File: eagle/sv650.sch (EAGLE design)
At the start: 31 parts, among them Q1 IRLML6344

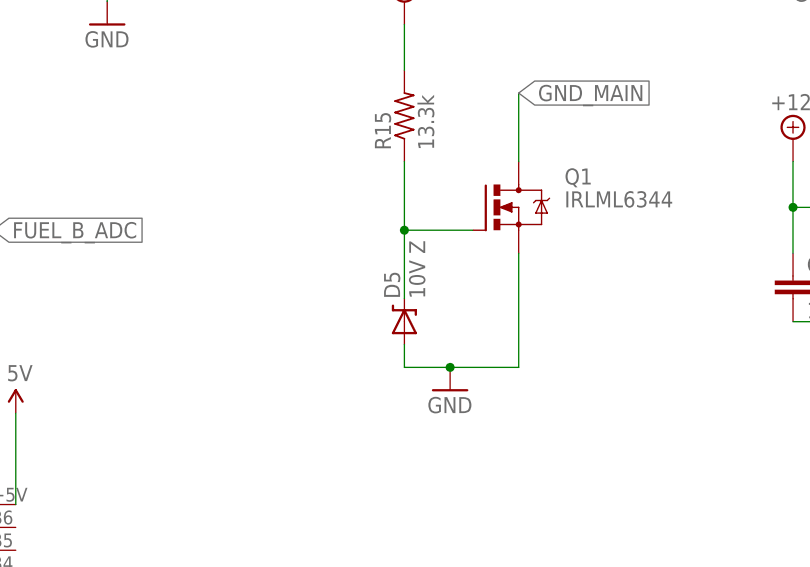
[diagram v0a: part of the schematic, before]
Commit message: switch D5 to a SOD-123 package
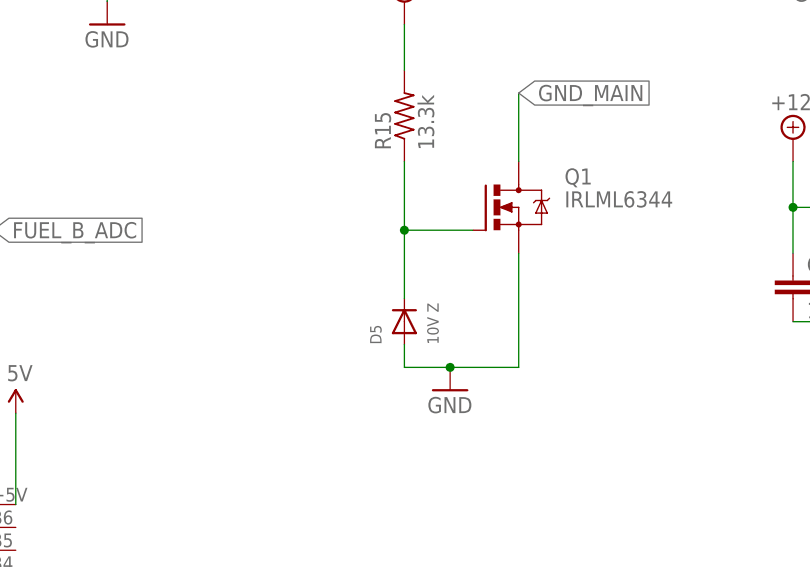
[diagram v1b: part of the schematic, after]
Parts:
- D5: device SparkFun-DiscreteSemi:DIODE-ZENER-BZT52 -> adafruit:DIODESOD-123
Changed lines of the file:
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@@
 <?xml version="1.0" encoding="utf-8"?>
 <!DOCTYPE eagle SYSTEM "eagle.dtd">
-<eagle version="6.5.0">
+<eagle version="7.1.0">
 <drawing>
 <settings>
@@
 <part name="R15" library="resistor" deviceset="R-US_" device="M0805" value="13.3k"/>
 <part name="SUPPLY5" library="supply2" deviceset="+12V" device=""/>
-<part name="D5" library="SparkFun-DiscreteSemi" deviceset="DIODE-ZENER" device="-BZT52" value="10V Z"/>
+<part name="D5" library="adafruit" deviceset="DIODE" device="SOD-123" value="10V Z"/>
 <part name="GND13" library="SparkFun" deviceset="GND" device=""/>
 </parts>

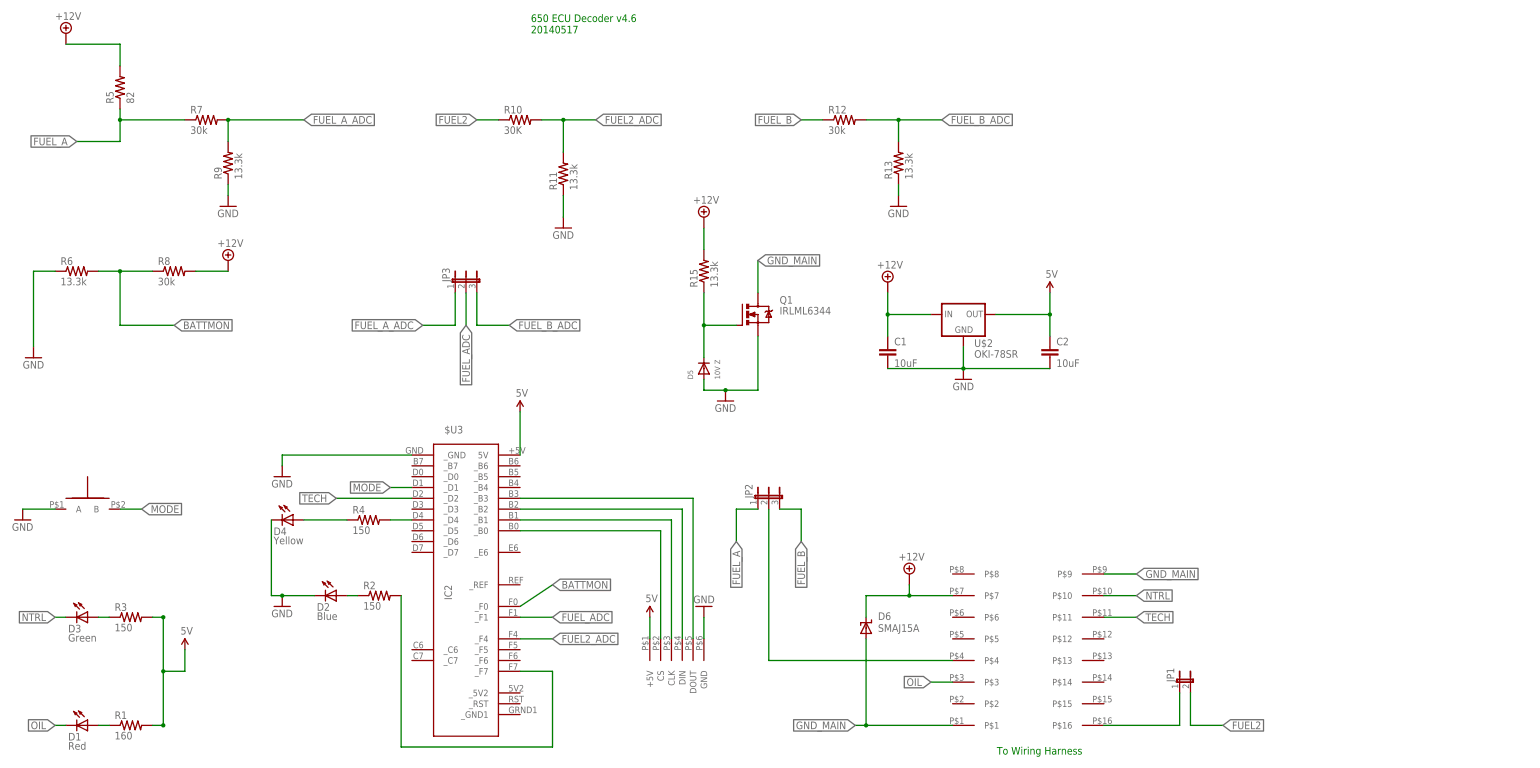
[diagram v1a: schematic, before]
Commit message: First pass at using Nokia LCD display
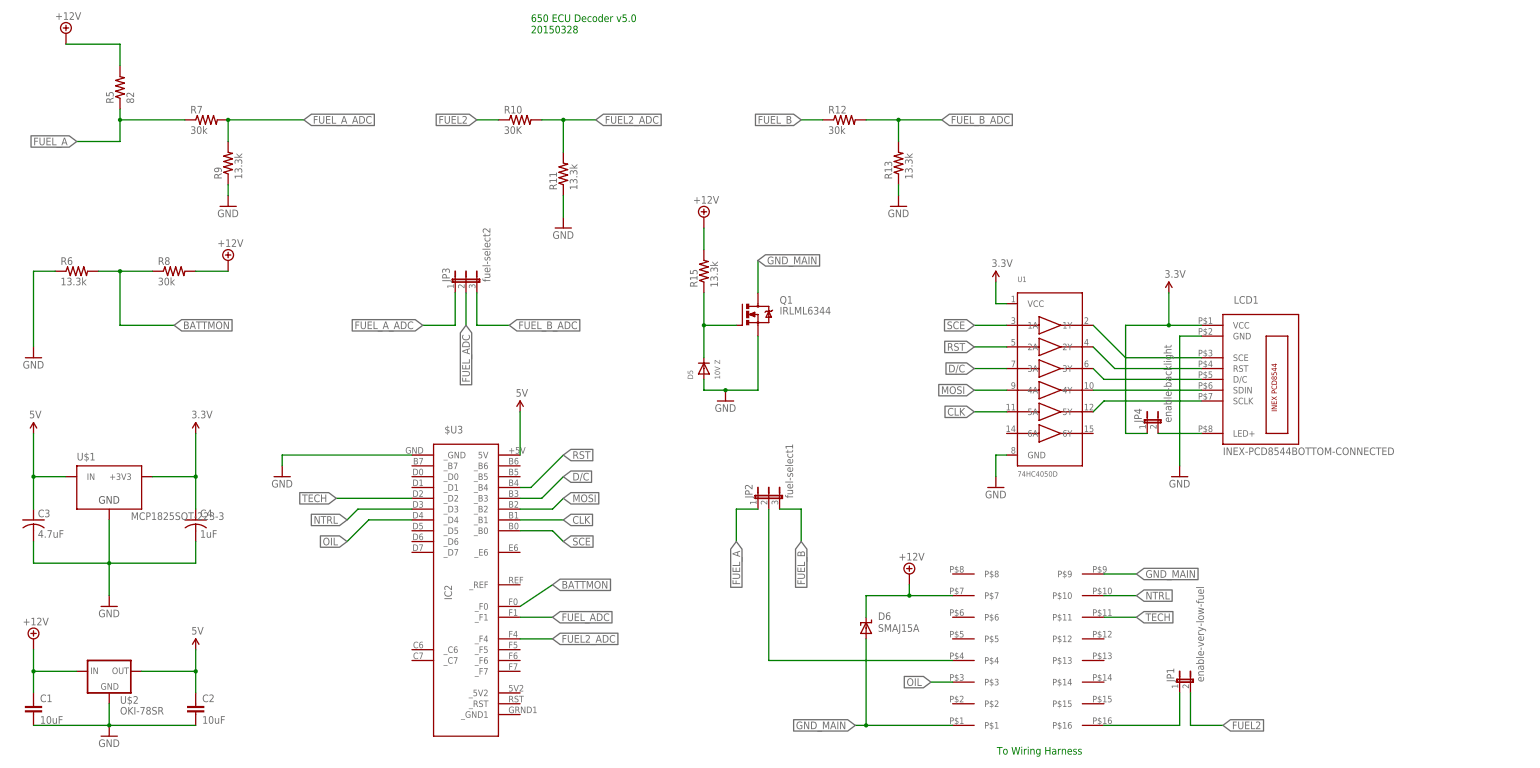
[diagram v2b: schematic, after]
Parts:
- removed D1: Red, led:LED10MM
- removed D2: Blue, led:LED5MM
- removed D3: Green, led:LED10MM
- removed D4: Yellow, led:LED10MM
- removed R1: 160, resistor:R-US_M0805
- removed R2, R3, R4: 150, resistor:R-US_M0805
- removed U$10: R13-509A-05-BB/R13-509A-05-BR, synfinatic:R13-509A-05-BB/R13-509A-05-BR
- added C3: 4.7uF, resistor:C-USC0805
- added C4: 1uF, resistor:C-USC0805
- added JP4: enable-backlight, jumper:JP1E
- added LCD1: INEX-PCD8544BOTTOM-CONNECTED, synfinatic:INEX-PCD8544BOTTOM-CONNECTED
- added U1: 74HC4050D, microbuilder:74HC4050D
- JP1: value (none) -> enable-very-low-fuel
- JP2: value (none) -> fuel-select1
- JP3: value (none) -> fuel-select2
- U$1: value OASIS-7-SEG-DISPLAY -> MCP1825SOT-223-3; device synfinatic:OASIS-7-SEG-DISPLAY -> synfinatic:MCP1825SOT-223-3; OC_NEWARK unknown -> (none)
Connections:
- removed net MODE: $U3._D1, U$10.B
- removed net N$3: $U3._B1, U$1.CLK
- removed net N$4: $U3._B2, U$1.DIN
- removed net N$5: $U3._B3, U$1.DOUT
- removed net N$6: D3.A, R3.1
- removed net N$7: D2.A, R2.1
- removed net R2: D4.A, R4.1
- new net 3.3V: C4.1, JP4.1, LCD1.VCC, U$1.+3V3, U1.VCC
- new net CLK: $U3._B1, U1.5A
- new net D/C: $U3._B3, U1.3A
- new net MOSI: $U3._B2, U1.4A
- new net N$13: LCD1.D/C, U1.3Y
- new net N$15: LCD1.SDIN, U1.4Y
- new net RST: $U3._B4, U1.2A
- new net SCE: $U3._B0, U1.1A
- net 5V: now also C3.1, U$1.IN; no longer R1.2, R3.2, U$1.+5V
- net GND: now also C3.2, C4.2, LCD1.GND, U1.GND; no longer D2.C, D4.C, U$10.A
- net N$16: now also LCD1.SCLK, U1.5Y; no longer $U3._F7, R2.2
- net N$2: now also JP4.2, LCD1.LED+; no longer $U3._B0, U$1.CS
- net N$8: now also LCD1.SCE, U1.1Y; no longer D1.A, R1.1
- net N$9: now also LCD1.RST, U1.2Y; no longer $U3._D4, R4.2
- net NTRL: now also $U3._D3; no longer D3.C
- net OIL: now also $U3._D4; no longer D1.C
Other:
- note added: "650 ECU Decoder v5.0 20150328"
- note removed: "650 ECU Decoder v4.6 20140517"
- moved on the sheet: C1, C2, U$2

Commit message: update board to have a 6mm switch on front
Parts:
- added S1: Mode, synfinatic:SWITCH-MOMENTARY-2
- LCD1: value INEX-PCD8544BOTTOM-CONNECTED -> INEX-PCD8544NOKIA-5110-EBAY-NOHOLES-BOTTOM; device synfinatic:INEX-PCD8544BOTTOM-CONNECTED -> synfinatic:INEX-PCD8544NOKIA-5110-EBAY-NOHOLES-BOTTOM
- renumbered U1 to U$5
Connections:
- new net N$3: $U3._D6, S1.2
- net GND: now also S1.1
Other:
- note added: "650 ECU Decoder v5.0 20150423"
- note removed: "650 ECU Decoder v5.0 20150328"
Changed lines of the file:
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@@
 <part name="U$6" library="SparkFun" deviceset="5V" device=""/>
 <part name="SUPPLY6" library="SparkFun-Aesthetics" deviceset="3.3V" device=""/>
-<part name="LCD1" library="synfinatic" deviceset="INEX-PCD8544" device="BOTTOM-CONNECTED" value="INEX-PCD8544BOTTOM-CONNECTED"/>
+<part name="LCD1" library="synfinatic" deviceset="INEX-PCD8544" device="NOKIA-5110-EBAY-NOHOLES-BOTTOM" value="INEX-PCD8544NOKIA-5110-EBAY-NOHOLES-BOTTOM"/>
 <part name="SUPPLY7" library="SparkFun-Aesthetics" deviceset="3.3V" device=""/>
 <part name="GND5" library="SparkFun" deviceset="GND" device=""/>
-<part name="U1" library="microbuilder" deviceset="74HC4050D" device="" value="74HC4050D"/>
+<part name="U$5" library="microbuilder" deviceset="74HC4050D" device="" value="74HC4050D"/>
 <part name="SUPPLY8" library="SparkFun-Aesthetics" deviceset="3.3V" device=""/>
 <part name="GND6" library="SparkFun" deviceset="GND" device=""/>
 <part name="JP4" library="jumper" deviceset="JP1E" device="" value="enable-backlight"/>
+<part name="S1" library="synfinatic" deviceset="SWITCH-MOMENTARY-2" device="" value="Mode"/>
+<part name="GND7" library="SparkFun" deviceset="GND" device=""/>
 </parts>
 <sheets>
@@
 <text x="157.48" y="-38.1" size="1.778" layer="91" rot="R180">To Wiring Harness</text>
 <text x="27.94" y="129.54" size="1.778" layer="91">650 ECU Decoder v5.0
-20150328</text>
+20150423</text>
 </plain>
 <instances>
@@
 <instance part="SUPPLY7" gate="G$1" x="177.8" y="68.58"/>
 <instance part="GND5" gate="1" x="180.34" y="25.4"/>
-<instance part="U1" gate="G$1" x="149.86" y="48.26"/>
+<instance part="U$5" gate="G$1" x="149.86" y="48.26"/>
 <instance part="SUPPLY8" gate="G$1" x="137.16" y="71.12"/>
 <instance part="GND6" gate="1" x="137.16" y="22.86"/>
 <instance part="JP4" gate="A" x="172.72" y="38.1"/>
+<instance part="S1" gate="G$1" x="-22.86" y="0" smashed="yes">
+<attribute name="NAME" x="-25.4" y="2.54" size="1.778" layer="95"/>
+</instance>
+<instance part="GND7" gate="1" x="-30.48" y="-7.62"/>
 </instances>
 <busses>
@@
 </segment>
 <segment>
-<pinref part="U1" gate="G$1" pin="GND"/>
+<pinref part="U$5" gate="G$1" pin="GND"/>
 <wire x1="139.7" y1="30.48" x2="137.16" y2="30.48" width="0.1524" layer="91"/>
 <wire x1="137.16" y1="30.48" x2="137.16" y2="25.4" width="0.1524" layer="91"/>
 <pinref part="GND6" gate="1" pin="GND"/>
+</segment>
+<segment>
+<pinref part="S1" gate="G$1" pin="1"/>
+<wire x1="-27.94" y1="0" x2="-30.48" y2="0" width="0.1524" layer="91"/>
+<wire x1="-30.48" y1="0" x2="-30.48" y2="-5.08" width="0.1524" layer="91"/>
+<pinref part="GND7" gate="1" pin="GND"/>
 </segment>
 </net>
@@
 </segment>
 <segment>
-<pinref part="U1" gate="G$1" pin="VCC"/>
+<pinref part="U$5" gate="G$1" pin="VCC"/>
 <wire x1="139.7" y1="66.04" x2="137.16" y2="66.04" width="0.1524" layer="91"/>
 <wire x1="137.16" y1="66.04" x2="137.16" y2="71.12" width="0.1524" layer="91"/>
@@
 <pinref part="LCD1" gate="G$1" pin="SCE"/>
 <wire x1="185.42" y1="53.34" x2="167.64" y2="53.34" width="0.1524" layer="91"/>
-<pinref part="U1" gate="G$1" pin="1Y"/>
+<pinref part="U$5" gate="G$1" pin="1Y"/>
 <wire x1="167.64" y1="53.34" x2="160.02" y2="60.96" width="0.1524" layer="91"/>
 </segment>
@@
 <pinref part="LCD1" gate="G$1" pin="RST"/>
 <wire x1="185.42" y1="50.8" x2="165.1" y2="50.8" width="0.1524" layer="91"/>
-<pinref part="U1" gate="G$1" pin="2Y"/>
+<pinref part="U$5" gate="G$1" pin="2Y"/>
 <wire x1="165.1" y1="50.8" x2="160.02" y2="55.88" width="0.1524" layer="91"/>
 </segment>
@@
 <pinref part="LCD1" gate="G$1" pin="D/C"/>
 <wire x1="185.42" y1="48.26" x2="162.56" y2="48.26" width="0.1524" layer="91"/>
-<pinref part="U1" gate="G$1" pin="3Y"/>
+<pinref part="U$5" gate="G$1" pin="3Y"/>
 <wire x1="162.56" y1="48.26" x2="160.02" y2="50.8" width="0.1524" layer="91"/>
 </segment>
@@
 <pinref part="LCD1" gate="G$1" pin="SDIN"/>
 <wire x1="185.42" y1="45.72" x2="160.02" y2="45.72" width="0.1524" layer="91"/>
-<pinref part="U1" gate="G$1" pin="4Y"/>
+<pinref part="U$5" gate="G$1" pin="4Y"/>
 </segment>
 </net>
@@
 <pinref part="LCD1" gate="G$1" pin="SCLK"/>
 <wire x1="185.42" y1="43.18" x2="162.56" y2="43.18" width="0.1524" layer="91"/>
-<pinref part="U1" gate="G$1" pin="5Y"/>
+<pinref part="U$5" gate="G$1" pin="5Y"/>
 <wire x1="162.56" y1="43.18" x2="160.02" y2="40.64" width="0.1524" layer="91"/>
 </segment>
@@
 </segment>
 <segment>
-<pinref part="U1" gate="G$1" pin="2A"/>
+<pinref part="U$5" gate="G$1" pin="2A"/>
 <wire x1="139.7" y1="55.88" x2="132.08" y2="55.88" width="0.1524" layer="91"/>
 <label x="132.08" y="55.88" size="1.778" layer="95" rot="R180" xref="yes"/>
@@
 </segment>
 <segment>
-<pinref part="U1" gate="G$1" pin="3A"/>
+<pinref part="U$5" gate="G$1" pin="3A"/>
 <wire x1="139.7" y1="50.8" x2="132.08" y2="50.8" width="0.1524" layer="91"/>
 <label x="132.08" y="50.8" size="1.778" layer="95" rot="R180" xref="yes"/>
@@
 </segment>
 <segment>
-<pinref part="U1" gate="G$1" pin="4A"/>
+<pinref part="U$5" gate="G$1" pin="4A"/>
 <wire x1="139.7" y1="45.72" x2="132.08" y2="45.72" width="0.1524" layer="91"/>
 <label x="132.08" y="45.72" size="1.778" layer="95" rot="R180" xref="yes"/>
@@
 </segment>
 <segment>
-<pinref part="U1" gate="G$1" pin="5A"/>
+<pinref part="U$5" gate="G$1" pin="5A"/>
 <wire x1="139.7" y1="40.64" x2="132.08" y2="40.64" width="0.1524" layer="91"/>
 <label x="132.08" y="40.64" size="1.778" layer="95" rot="R180" xref="yes"/>
@@
 </segment>
 <segment>
-<pinref part="U1" gate="G$1" pin="1A"/>
+<pinref part="U$5" gate="G$1" pin="1A"/>
 <wire x1="139.7" y1="60.96" x2="132.08" y2="60.96" width="0.1524" layer="91"/>
 <label x="132.08" y="60.96" size="1.778" layer="95" rot="R180" xref="yes"/>
@@
 </segment>
 </net>
+<net name="N$3" class="0">
+<segment>
+<pinref part="$U3" gate="G$1" pin="_D6"/>
+<pinref part="S1" gate="G$1" pin="2"/>
+<wire x1="0" y1="10.16" x2="-7.62" y2="10.16" width="0.1524" layer="91"/>
+<wire x1="-7.62" y1="10.16" x2="-17.78" y2="0" width="0.1524" layer="91"/>
+</segment>
+</net>

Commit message: v5.0 board with Nokia 5110 LCD screen
as ordered from OSHPark
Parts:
- removed R12: 30k, resistor:R-US_M0805
- removed R13, R15: 13.3k, resistor:R-US_M0805
- added R1: 82, synfinatic:RESISTORPTH-5W
- added R2: 13.3k, resistor:R-US_M0805
- added R3: 30K, resistor:R-US_M0805
- R10: value 30K -> 13.3k
- R5: value 82 -> 30k; device synfinatic:RESISTORPTH-5W -> resistor:R-US_M0805
- R6: MF VISHAY/DALE -> (none); MPN CRCW080510K0FKTA -> (none); OC_NEWARK 05F1511 -> (none)
- R9: MF (none) -> VISHAY/DALE; MPN (none) -> CRCW080510K0FKTA; OC_NEWARK (none) -> 05F1511
- renumbered D5 to D1, D6 to D2, R11 to R4
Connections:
- net +12V: now also R1.2, R10.2; no longer R15.2, R5.2
- net BATTMON: now also R9.2; no longer R6.2
- net FUEL2: now also R3.1; no longer R10.1
- net FUEL2_ADC: now also R3.2; no longer R10.2
- net FUEL_A: now also R1.1; no longer R5.1
- net FUEL_A_ADC: now also R2.2; no longer R9.2
- net FUEL_B: now also R5.1; no longer R12.1
- net FUEL_B_ADC: now also R5.2, R6.2; no longer R12.2, R13.2
- net GND: now also R2.1, U$5.6A; no longer R13.1
- net N$17: now also R10.1; no longer R15.1
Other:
- note added: "650 ECU Decoder v5.0 20150425"
- note removed: "650 ECU Decoder v5.0 20150423"
- moved on the sheet: R10, R5, R6, R9
